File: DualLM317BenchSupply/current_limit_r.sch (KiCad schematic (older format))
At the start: 13 parts

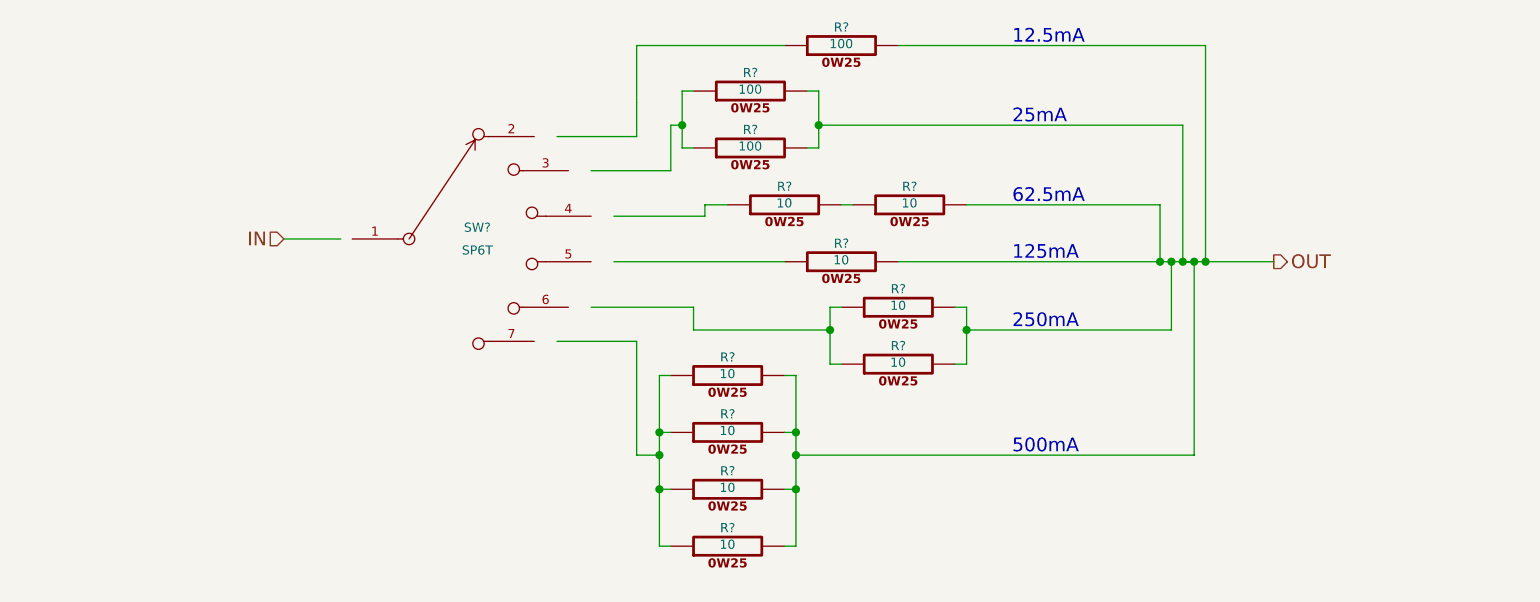
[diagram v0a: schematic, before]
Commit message: adding input / output switches, revising schematic parts.
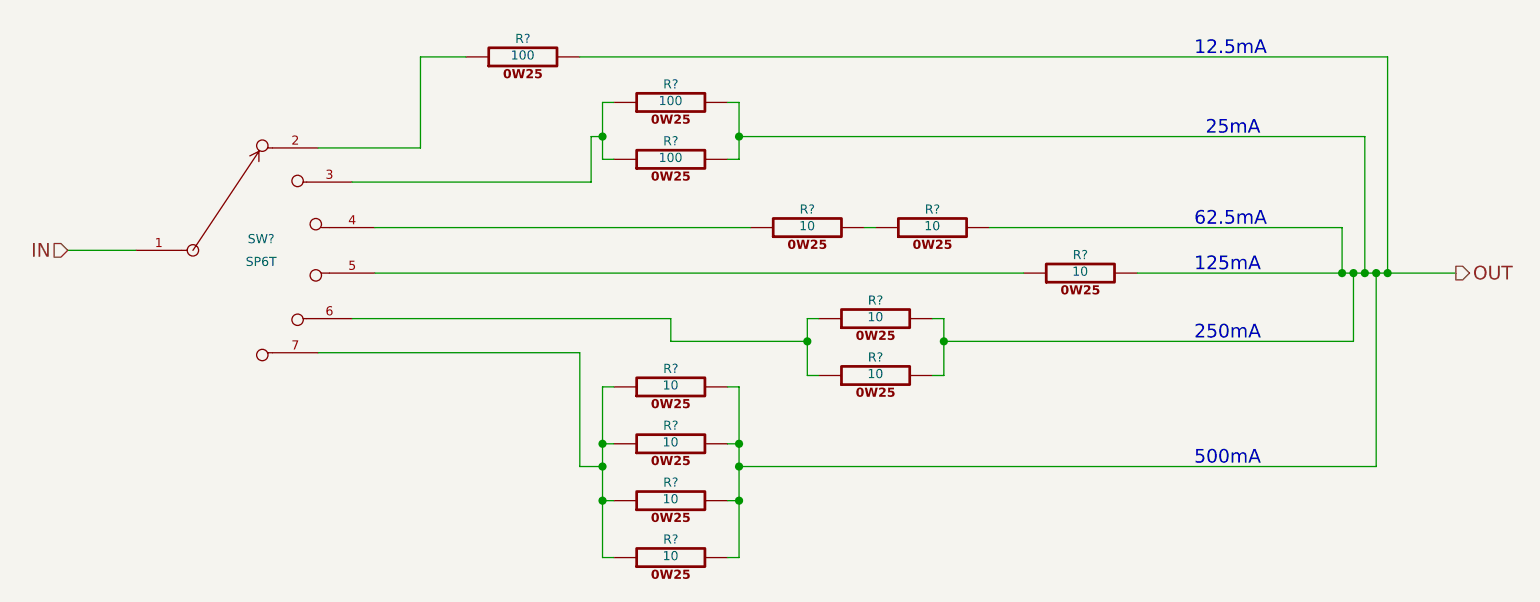
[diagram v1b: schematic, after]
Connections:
- wire segments 72 -> 64
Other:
- moved on the sheet: R?, SW?

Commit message: annotating parts.  adding printout of schematic.
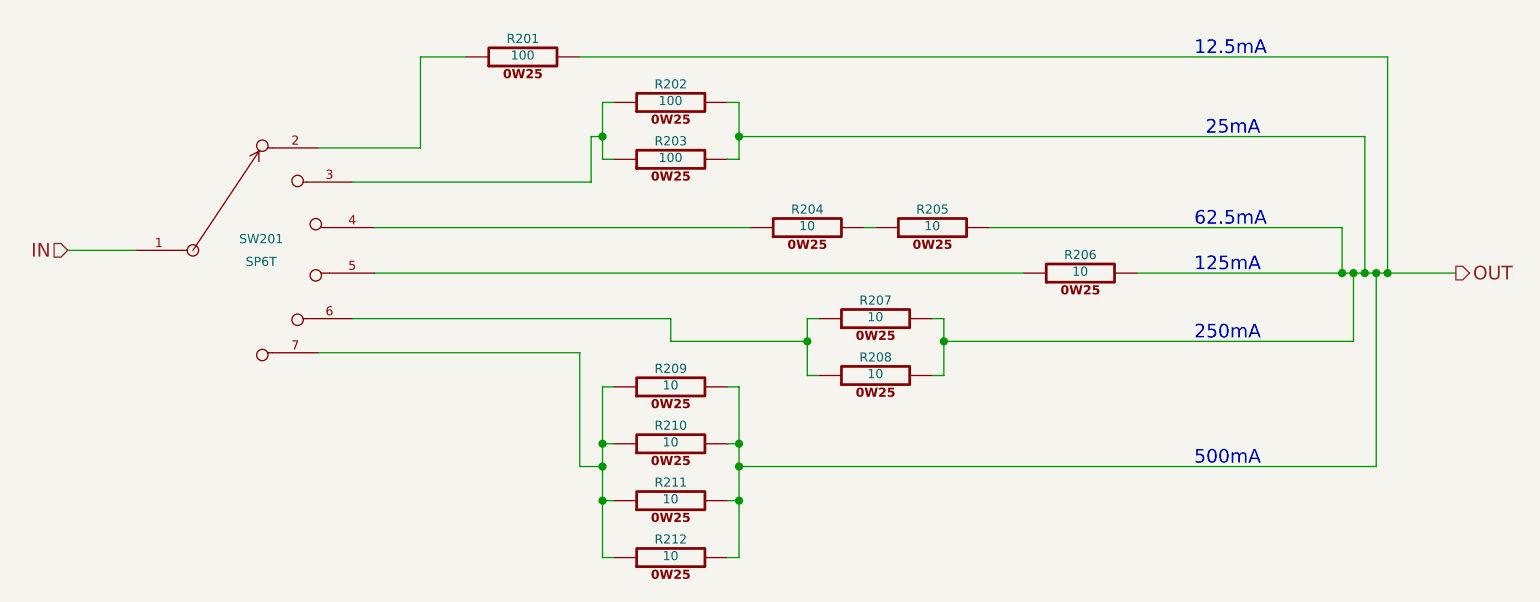
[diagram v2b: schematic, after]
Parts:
- gave numbers to parts that had none: 13
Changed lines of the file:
@@
 $EndDescr
 $Comp
-L R_0W25 R?
+L R_0W25 R206
 U 1 1 53253757
 P 7000 3900
-F 0 "R?" V 7080 3900 40  0000 C CNN
+F 0 "R206" V 7080 3900 40  0000 C CNN
 F 1 "10" V 7007 3901 40  0000 C CNN
 F 2 "~" V 6930 3900 30  0000 C CNN
@@
 $EndComp
 $Comp
-L R_0W25 R?
+L R_0W25 R204
 U 1 1 5325375D
 P 5800 3700
-F 0 "R?" V 5880 3700 40  0000 C CNN
+F 0 "R204" V 5880 3700 40  0000 C CNN
 F 1 "10" V 5807 3701 40  0000 C CNN
 F 2 "~" V 5730 3700 30  0000 C CNN
@@
 $EndComp
 $Comp
-L R_0W25 R?
+L R_0W25 R205
 U 1 1 53253763
 P 6350 3700
-F 0 "R?" V 6430 3700 40  0000 C CNN
+F 0 "R205" V 6430 3700 40  0000 C CNN
 F 1 "10" V 6357 3701 40  0000 C CNN
 F 2 "~" V 6280 3700 30  0000 C CNN
@@
 $EndComp
 $Comp
-L R_0W25 R?
+L R_0W25 R207
 U 1 1 53253769
 P 6100 4100
-F 0 "R?" V 6180 4100 40  0000 C CNN
+F 0 "R207" V 6180 4100 40  0000 C CNN
 F 1 "10" V 6107 4101 40  0000 C CNN
 F 2 "~" V 6030 4100 30  0000 C CNN
@@
 $EndComp
 $Comp
-L R_0W25 R?
+L R_0W25 R208
 U 1 1 5325376F
 P 6100 4350
-F 0 "R?" V 6180 4350 40  0000 C CNN
+F 0 "R208" V 6180 4350 40  0000 C CNN
 F 1 "10" V 6107 4351 40  0000 C CNN
 F 2 "~" V 6030 4350 30  0000 C CNN
@@
 $EndComp
 $Comp
-L R_0W25 R?
+L R_0W25 R209
 U 1 1 53253775
 P 5200 4400
-F 0 "R?" V 5280 4400 40  0000 C CNN
+F 0 "R209" V 5280 4400 40  0000 C CNN
 F 1 "10" V 5207 4401 40  0000 C CNN
 F 2 "~" V 5130 4400 30  0000 C CNN
@@
 $EndComp
 $Comp
-L R_0W25 R?
+L R_0W25 R210
 U 1 1 5325377B
 P 5200 4650
-F 0 "R?" V 5280 4650 40  0000 C CNN
+F 0 "R210" V 5280 4650 40  0000 C CNN
 F 1 "10" V 5207 4651 40  0000 C CNN
 F 2 "~" V 5130 4650 30  0000 C CNN
@@
 $EndComp
 $Comp
-L R_0W25 R?
+L R_0W25 R211
 U 1 1 53253781
 P 5200 4900
-F 0 "R?" V 5280 4900 40  0000 C CNN
+F 0 "R211" V 5280 4900 40  0000 C CNN
 F 1 "10" V 5207 4901 40  0000 C CNN
 F 2 "~" V 5130 4900 30  0000 C CNN
@@
 $EndComp
 $Comp
-L R_0W25 R?
+L R_0W25 R212
 U 1 1 53253787
 P 5200 5150
-F 0 "R?" V 5280 5150 40  0000 C CNN
+F 0 "R212" V 5280 5150 40  0000 C CNN
 F 1 "10" V 5207 5151 40  0000 C CNN
 F 2 "~" V 5130 5150 30  0000 C CNN
@@
 Connection ~ 4900 4650
 $Comp
-L SP6T SW?
+L SP6T SW201
 U 1 1 53253794
 P 3100 3800
-F 0 "SW?" H 3400 3850 40  0000 C CNN
+F 0 "SW201" H 3400 3850 40  0000 C CNN
 F 1 "SP6T" H 3400 3750 40  0000 C CNN
 F 2 "~" H 3100 4800 60  0000 C CNN
@@
 	6100 3700 6050 3700
 $Comp
-L R_0W25 R?
+L R_0W25 R203
 U 1 1 532537AA
 P 5200 3400
-F 0 "R?" V 5280 3400 40  0000 C CNN
+F 0 "R203" V 5280 3400 40  0000 C CNN
 F 1 "100" V 5207 3401 40  0000 C CNN
 F 2 "~" V 5130 3400 30  0000 C CNN
@@
 $EndComp
 $Comp
-L R_0W25 R?
+L R_0W25 R202
 U 1 1 532537B0
 P 5200 3150
-F 0 "R?" V 5280 3150 40  0000 C CNN
+F 0 "R202" V 5280 3150 40  0000 C CNN
 F 1 "100" V 5207 3151 40  0000 C CNN
 F 2 "~" V 5130 3150 30  0000 C CNN
@@
 $EndComp
 $Comp
-L R_0W25 R?
+L R_0W25 R201
 U 1 1 532537B6
 P 4550 2950
-F 0 "R?" V 4630 2950 40  0000 C CNN
+F 0 "R201" V 4630 2950 40  0000 C CNN
 F 1 "100" V 4557 2951 40  0000 C CNN
 F 2 "~" V 4480 2950 30  0000 C CNN

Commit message: adding connectors and heatsinks libs
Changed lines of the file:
@@
 	4950 4400 4900 4400
 Wire Wire Line
-	4900 4400 4900 4650
-Wire Wire Line
-	4900 4650 4900 4750
-Wire Wire Line
-	4900 4750 4900 4900
-Wire Wire Line
-	4900 4900 4900 5150
+	4900 4400 4900 5150
 Wire Wire Line
 	4900 5150 4950 5150
@@
 	5800 4350 5850 4350
 Wire Wire Line
-	5800 4100 5800 4200
-Wire Wire Line
-	5800 4200 5800 4350
+	5800 4100 5800 4350
 Wire Wire Line
 	5800 4100 5850 4100
@@
 	4950 3150 4900 3150
 Wire Wire Line
-	4900 3150 4900 3300
-Wire Wire Line
-	4900 3300 4900 3400
+	4900 3150 4900 3400
 Wire Wire Line
 	4900 3400 4950 3400
@@
 	6350 4100 6400 4100
 Wire Wire Line
-	6400 4100 6400 4200
-Wire Wire Line
-	6400 4200 6400 4350
+	6400 4100 6400 4350
 Wire Wire Line
 	6400 4350 6350 4350
@@
 	5450 3150 5500 3150
 Wire Wire Line
-	5500 3150 5500 3300
-Wire Wire Line
-	5500 3300 5500 3400
+	5500 3150 5500 3400
 Wire Wire Line
 	5500 3400 5450 3400
@@
 	5450 4400 5500 4400
 Wire Wire Line
-	5500 4400 5500 4650
-Wire Wire Line
-	5500 4650 5500 4750
-Wire Wire Line
-	5500 4750 5500 4900
-Wire Wire Line
-	5500 4900 5500 5150
+	5500 4400 5500 5150
 Wire Wire Line
 	5500 5150 5450 5150
@@
 Connection ~ 5500 4650
 Wire Wire Line
-	7250 3900 8150 3900
-Wire Wire Line
-	8150 3900 8200 3900
-Wire Wire Line
-	8200 3900 8250 3900
-Wire Wire Line
-	8250 3900 8300 3900
-Wire Wire Line
-	8300 3900 8350 3900
-Wire Wire Line
-	8350 3900 8650 3900
+	7250 3900 8650 3900
 Wire Wire Line
 	6600 3700 8150 3700
